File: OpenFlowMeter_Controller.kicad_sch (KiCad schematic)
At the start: 31 parts, among them J3 Conn_01x06, J5 Conn_01x03, J6 Conn_02x04_Odd_Even, J7 Conn_02x03_Odd_Even, U2 STM32F103C8Tx, U5 SN65HVD231, U7 24LC64, Y1 12 MHz

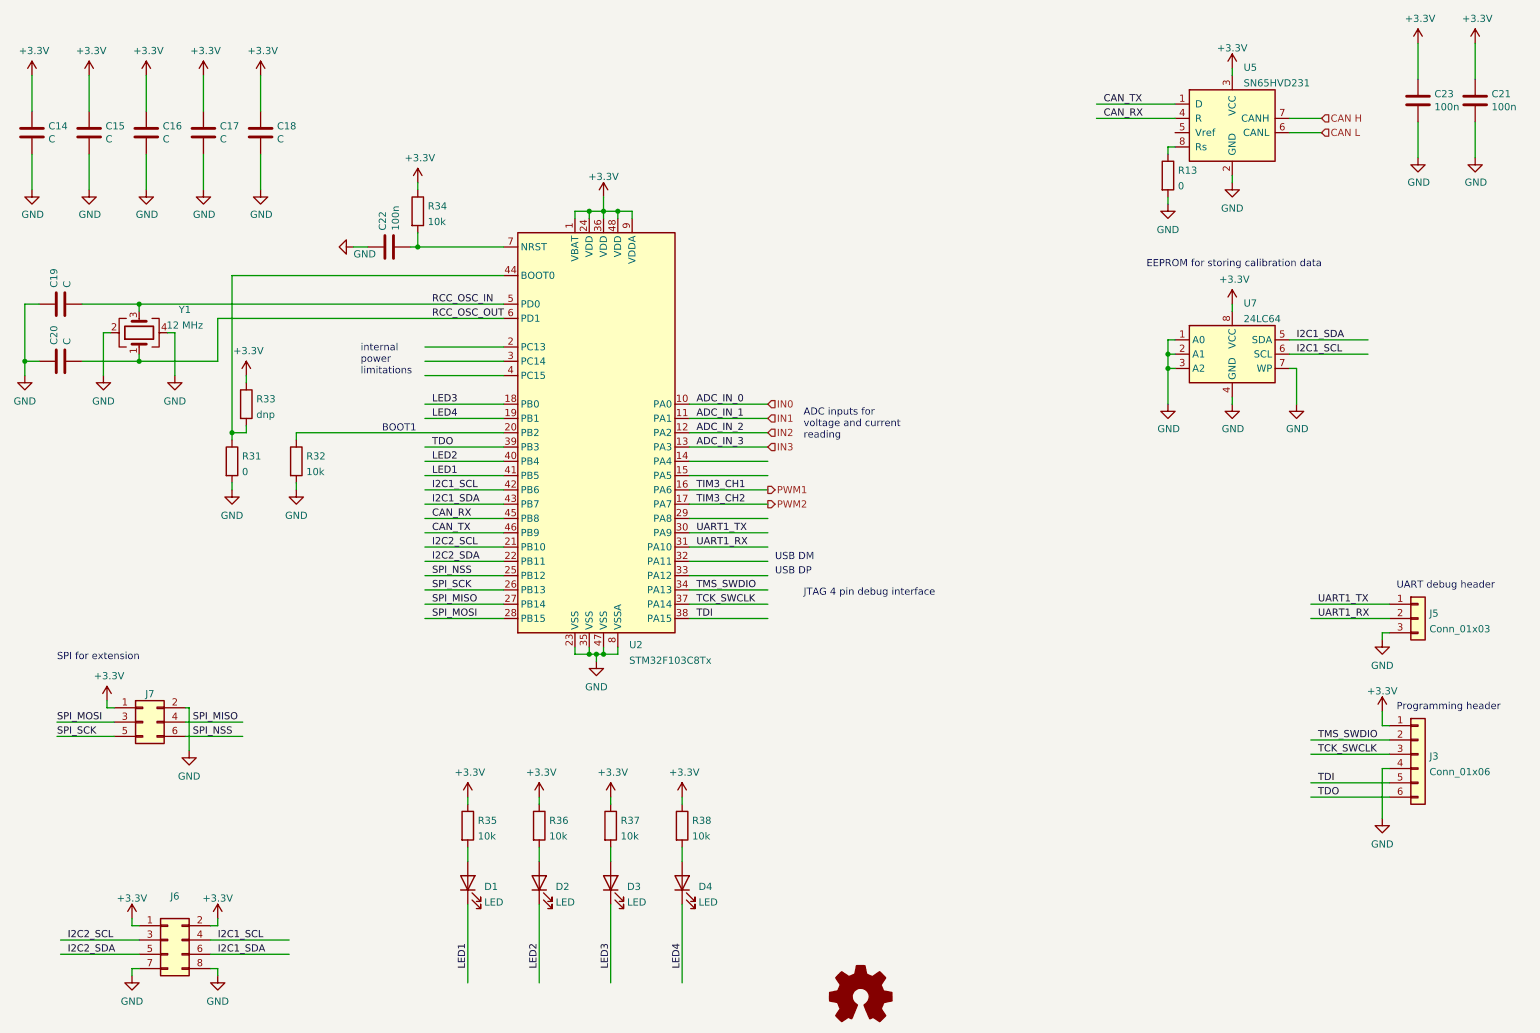
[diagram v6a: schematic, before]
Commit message: fixed layout
Fixed layout to host lager amplifier footprints.
Still some DRC warnings, but mostly regarding Silkscreen / Soldermask issues.
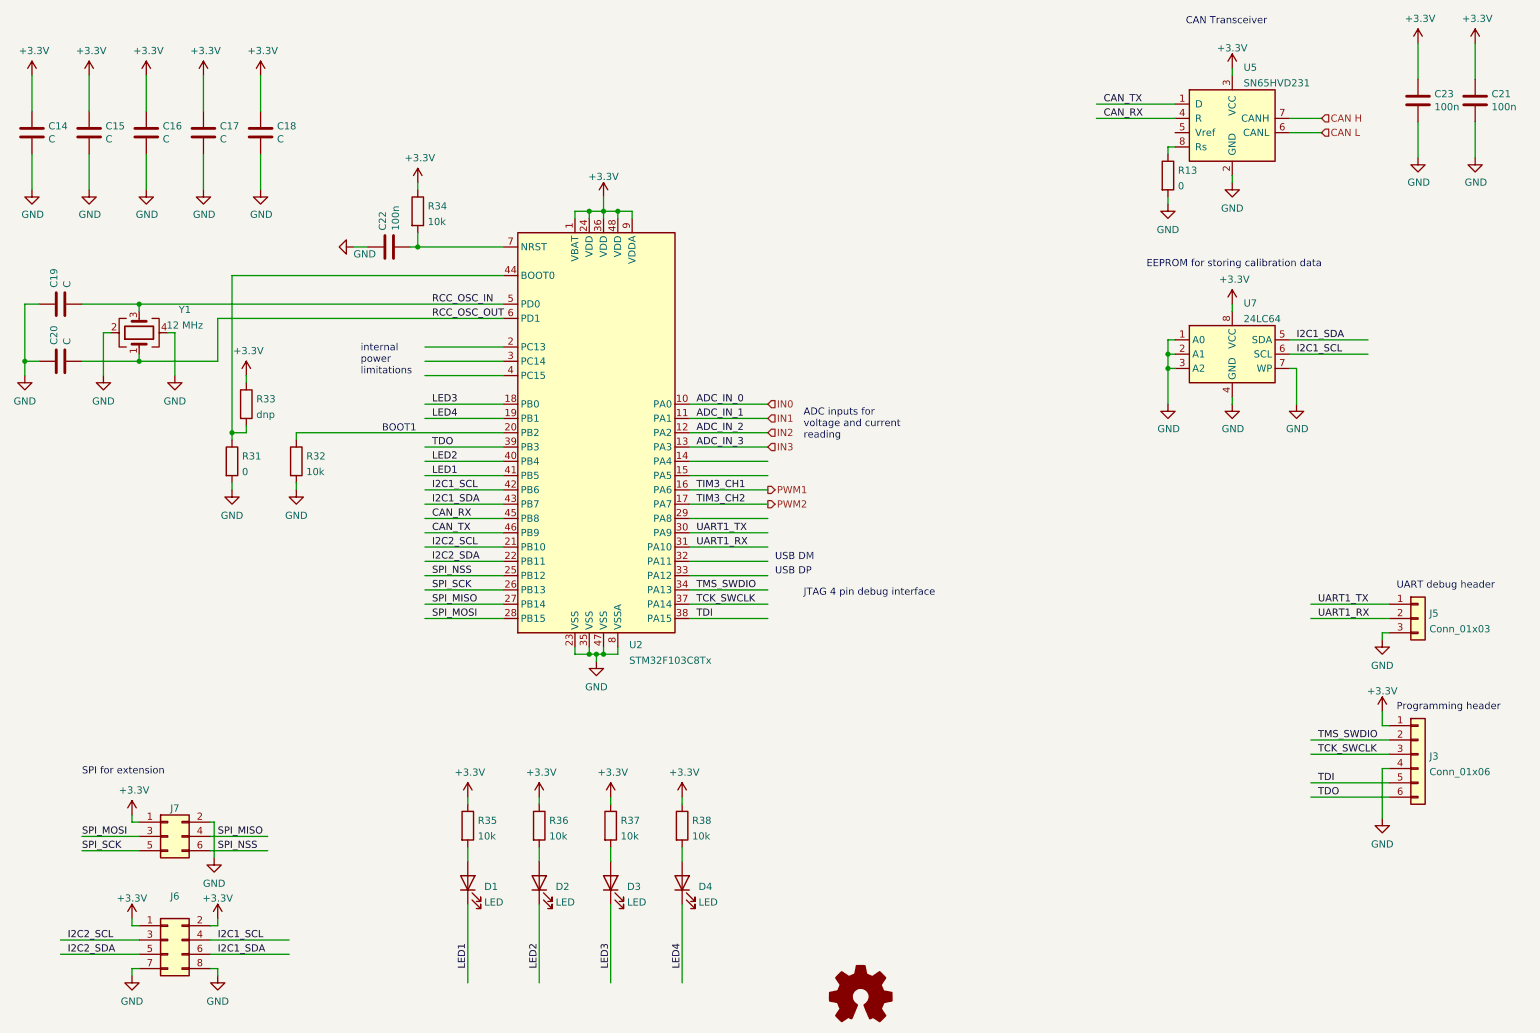
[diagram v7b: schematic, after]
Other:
- note added: "CAN Transceiver"
- moved on the sheet: J7
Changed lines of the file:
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@@
     (stroke (width 0) (type default) (color 0 0 0 0))
   )
-  (wire (pts (xy 46.355 142.875) (xy 56.515 142.875))
-    (stroke (width 0) (type default) (color 0 0 0 0))
-  )
-  (wire (pts (xy 46.355 140.335) (xy 56.515 140.335))
+  (wire (pts (xy 50.8 163.195) (xy 60.96 163.195))
+    (stroke (width 0) (type default) (color 0 0 0 0))
+  )
+  (wire (pts (xy 50.8 160.655) (xy 60.96 160.655))
     (stroke (width 0) (type default) (color 0 0 0 0))
   )
@@
     (stroke (width 0) (type default) (color 0 0 0 0))
   )
-  (wire (pts (xy 46.99 137.795) (xy 46.99 145.415))
+  (wire (pts (xy 51.435 158.115) (xy 51.435 164.465))
     (stroke (width 0) (type default) (color 0 0 0 0))
   )
@@
     (stroke (width 0) (type default) (color 0 0 0 0))
   )
-  (wire (pts (xy 32.385 137.795) (xy 33.655 137.795))
+  (wire (pts (xy 36.83 158.115) (xy 38.1 158.115))
     (stroke (width 0) (type default) (color 0 0 0 0))
   )
@@
     (stroke (width 0) (type default) (color 0 0 0 0))
   )
-  (wire (pts (xy 23.495 140.335) (xy 33.655 140.335))
+  (wire (pts (xy 27.94 160.655) (xy 38.1 160.655))
     (stroke (width 0) (type default) (color 0 0 0 0))
   )
@@
     (stroke (width 0) (type default) (color 0 0 0 0))
   )
-  (wire (pts (xy 46.355 137.795) (xy 46.99 137.795))
+  (wire (pts (xy 50.8 158.115) (xy 51.435 158.115))
     (stroke (width 0) (type default) (color 0 0 0 0))
   )
@@
     (stroke (width 0) (type default) (color 0 0 0 0))
   )
-  (wire (pts (xy 23.495 142.875) (xy 33.655 142.875))
+  (wire (pts (xy 27.94 163.195) (xy 38.1 163.195))
     (stroke (width 0) (type default) (color 0 0 0 0))
   )
@@
     (stroke (width 0) (type default) (color 0 0 0 0))
   )
-  (wire (pts (xy 32.385 136.525) (xy 32.385 137.795))
+  (wire (pts (xy 36.83 156.845) (xy 36.83 158.115))
     (stroke (width 0) (type default) (color 0 0 0 0))
   )
@@
     (effects (font (size 1.27 1.27)) (justify left bottom))
   )
-  (text "SPI for extension" (at 23.495 129.54 0)
+  (text "SPI for extension" (at 27.94 149.86 0)
     (effects (font (size 1.27 1.27)) (justify left bottom))
   )
@@
     (effects (font (size 1.27 1.27)) (justify left bottom))
   )
+  (text "CAN Transceiver" (at 224.155 16.51 0)
+    (effects (font (size 1.27 1.27)) (justify left bottom))
+  )
   (text "USB DP" (at 151.13 114.3 0)
     (effects (font (size 1.27 1.27)) (justify left bottom))
@@
     (effects (font (size 1.27 1.27)) (justify left bottom))
   )
-  (label "SPI_SCK" (at 23.495 142.875 0)
+  (label "SPI_SCK" (at 27.94 163.195 0)
     (effects (font (size 1.27 1.27)) (justify left bottom))
   )
@@
     (effects (font (size 1.27 1.27)) (justify left bottom))
   )
-  (label "SPI_MISO" (at 47.625 140.335 0)
+  (label "SPI_MISO" (at 52.07 160.655 0)
     (effects (font (size 1.27 1.27)) (justify left bottom))
   )
@@
     (effects (font (size 1.27 1.27)) (justify left bottom))
   )
-  (label "SPI_NSS" (at 47.625 142.875 0)
+  (label "SPI_NSS" (at 52.07 163.195 0)
     (effects (font (size 1.27 1.27)) (justify left bottom))
   )
@@
     (effects (font (size 1.27 1.27)) (justify left bottom))
   )
-  (label "SPI_MOSI" (at 23.495 140.335 0)
+  (label "SPI_MOSI" (at 27.94 160.655 0)
     (effects (font (size 1.27 1.27)) (justify left bottom))
   )
@@
     (pin "2")
   )
-  (symbol (lib_id "Connector_Generic:Conn_02x03_Odd_Even") (at 38.735 140.335 0) (unit 1)
-    (in_bom yes) (on_board yes) (fields_autoplaced)
-    (property "Reference" "J7" (id 0) (at 40.005 135.3335 0))
-    (property "Value" "Conn_02x03_Odd_Even" (id 1) (at 40.005 135.3336 0)
-      (effects (font (size 1.27 1.27)) hide)
-    )
-    (property "Footprint" "Connector_PinHeader_2.54mm:PinHeader_2x03_P2.54mm_Vertical_SMD" (id 2) (at 38.735 140.335 0)
-      (effects (font (size 1.27 1.27)) hide)
-    )
-    (property "Datasheet" "~" (id 3) (at 38.735 140.335 0)
+  (symbol (lib_id "Connector_Generic:Conn_02x03_Odd_Even") (at 43.18 160.655 0) (unit 1)
+    (in_bom yes) (on_board yes) (fields_autoplaced)
+    (property "Reference" "J7" (id 0) (at 44.45 155.6535 0))
+    (property "Value" "Conn_02x03_Odd_Even" (id 1) (at 44.45 155.6536 0)
+      (effects (font (size 1.27 1.27)) hide)
+    )
+    (property "Footprint" "Connector_PinHeader_2.54mm:PinHeader_2x03_P2.54mm_Vertical_SMD" (id 2) (at 43.18 160.655 0)
+      (effects (font (size 1.27 1.27)) hide)
+    )
+    (property "Datasheet" "~" (id 3) (at 43.18 160.655 0)
       (effects (font (size 1.27 1.27)) hide)
     )
@@
     (pin "2")
   )
-  (symbol (lib_id "power:GND") (at 46.99 145.415 0) (unit 1)
-    (in_bom yes) (on_board yes) (fields_autoplaced)
-    (property "Reference" "#PWR0121" (id 0) (at 46.99 151.765 0)
-      (effects (font (size 1.27 1.27)) hide)
-    )
-    (property "Value" "GND" (id 1) (at 46.99 149.9775 0))
-    (property "Footprint" "" (id 2) (at 46.99 145.415 0)
-      (effects (font (size 1.27 1.27)) hide)
-    )
-    (property "Datasheet" "" (id 3) (at 46.99 145.415 0)
+  (symbol (lib_id "power:GND") (at 51.435 164.465 0) (unit 1)
+    (in_bom yes) (on_board yes) (fields_autoplaced)
+    (property "Reference" "#PWR0121" (id 0) (at 51.435 170.815 0)
+      (effects (font (size 1.27 1.27)) hide)
+    )
+    (property "Value" "GND" (id 1) (at 51.435 169.0275 0))
+    (property "Footprint" "" (id 2) (at 51.435 164.465 0)
+      (effects (font (size 1.27 1.27)) hide)
+    )
+    (property "Datasheet" "" (id 3) (at 51.435 164.465 0)
       (effects (font (size 1.27 1.27)) hide)
     )
@@
     (pin "1")
   )
-  (symbol (lib_id "power:+3.3V") (at 32.385 136.525 0) (unit 1)
-    (in_bom yes) (on_board yes)
-    (property "Reference" "#PWR064" (id 0) (at 32.385 140.335 0)
-      (effects (font (size 1.27 1.27)) hide)
-    )
-    (property "Value" "+3.3V" (id 1) (at 32.766 132.1308 0))
-    (property "Footprint" "" (id 2) (at 32.385 136.525 0)
-      (effects (font (size 1.27 1.27)) hide)
-    )
-    (property "Datasheet" "" (id 3) (at 32.385 136.525 0)
-      (effects (font (size 1.27 1.27)) hide)
-    )
+  (symbol (lib_id "power:+3.3V") (at 36.83 156.845 0) (unit 1)
+    (in_bom yes) (on_board yes)
+    (property "Reference" "#PWR064" (id 0) (at 36.83 160.655 0)
+      (effects (font (size 1.27 1.27)) hide)
+    )
+    (property "Value" "+3.3V" (id 1) (at 37.211 152.4508 0))
+    (property "Footprint" "" (id 2) (at 36.83 156.845 0)
+      (effects (font (size 1.27 1.27)) hide)
+    )
+    (property "Datasheet" "" (id 3) (at 36.83 156.845 0)
+      (effects (font (size 1.27 1.27)) hide)
+    )
